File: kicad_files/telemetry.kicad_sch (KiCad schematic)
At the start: 24 parts, among them J10 Conn_ARM_JTAG_SWD_10, J4 RFD900ux 10 Pin Header, J5 RFD900ux 3 Pin Power Select, J6 USB_C_Receptacle_USB2.0_16P, U8 74AHCT125, U9 WE-TVS-82400102

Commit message: reset symbol annotations
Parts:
- renumbered C49 to C43, C52 to C44, C53 to C45, C54 to C46, C55 to C47, C56 to C48, C57 to C49, J4 to J3, J10 to J4, R12 to R10, R13 to R11, R14 to R12, R16 to R13, R17 to R14

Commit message: make schematic changes
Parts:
- removed U8: 74AHCT125, Package_SO:SOIC-14_3.9x8.7mm_P1.27mm, symbol 74xx:74AHCT125
- added U13: 74LVC1G125, Package_TO_SOT_SMD:SOT-23-5, symbol 74xGxx:74LVC1G125
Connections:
- net +5V: now also U13.5 (VCC)
- net GND: now also U13.1, U13.3 (GND)
- net LED_TIM2_CH1: now also U13.2
- net at R10.1: now also U13.4
- no-connect marks 8 -> 5
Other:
- moved on the sheet: C43, C44, D2, D3, R10

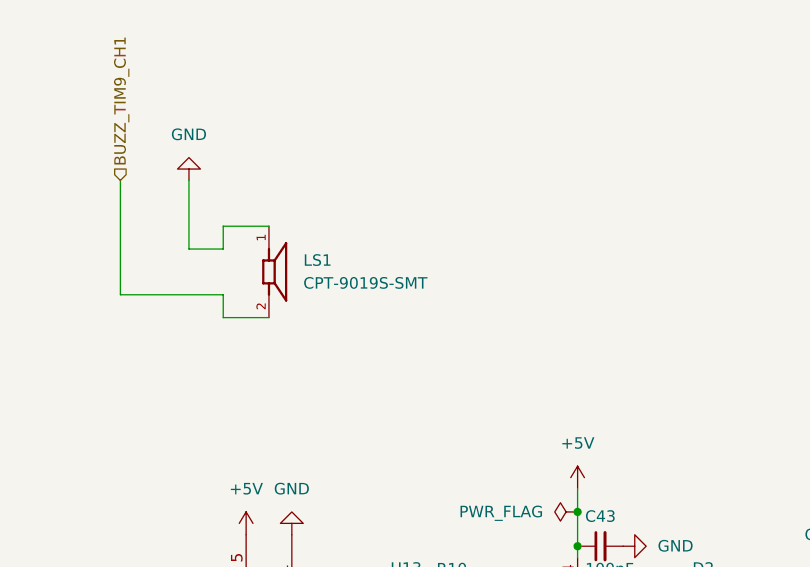
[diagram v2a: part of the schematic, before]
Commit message: Switch buzzer p/n
No footprint yet
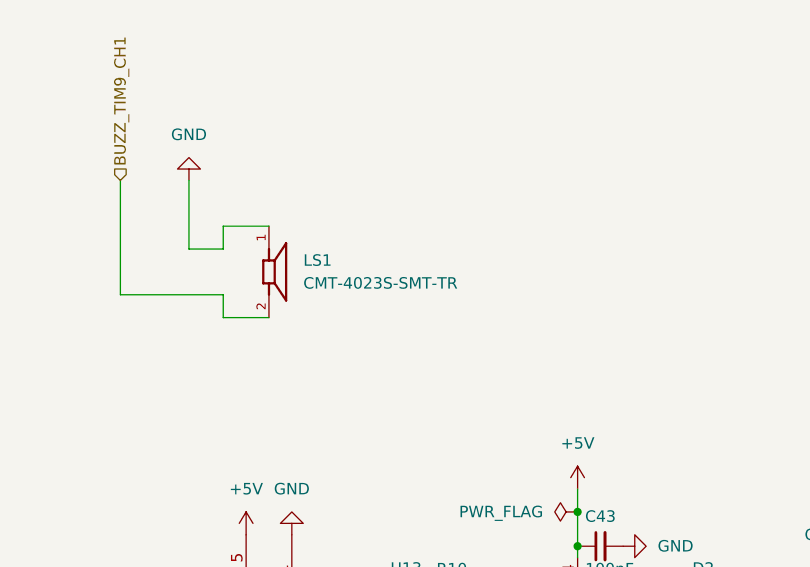
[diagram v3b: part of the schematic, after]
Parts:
- LS1: value CPT-9019S-SMT -> CMT-4023S-SMT-TR; footprint footprints:CUI_CPT-9019S-SMT -> (none)
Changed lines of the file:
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@@
 			)
 		)
-		(property "Value" "CPT-9019S-SMT"
+		(property "Value" "CMT-4023S-SMT-TR"
 			(at 49.53 48.2599 0)
 			(show_name no)
@@
 			)
 		)
-		(property "Footprint" "footprints:CUI_CPT-9019S-SMT"
+		(property "Footprint" ""
 			(at 45.72 46.99 0)
 			(hide yes)

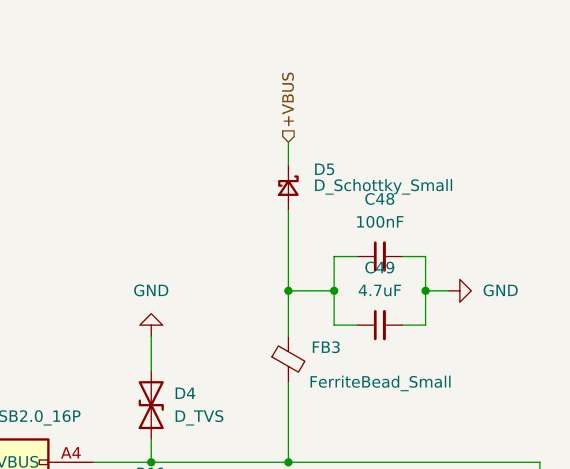
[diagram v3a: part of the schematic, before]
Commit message: VBUS, BMS diodes and fuses
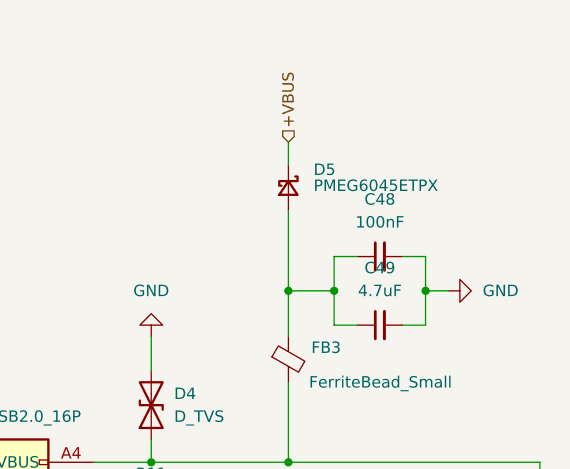
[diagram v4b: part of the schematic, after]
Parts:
- D5: value D_Schottky_Small -> PMEG6045ETPX; footprint (none) -> Diode_SMD:D_SOD-128
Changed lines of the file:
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@@
 			)
 		)
-		(property "Value" "D_Schottky_Small"
+		(property "Value" "PMEG6045ETPX"
 			(at 241.554 36.576 90)
 			(show_name no)
@@
 			)
 		)
-		(property "Footprint" ""
+		(property "Footprint" "Diode_SMD:D_SOD-128"
 			(at 238.76 36.83 90)
 			(hide yes)

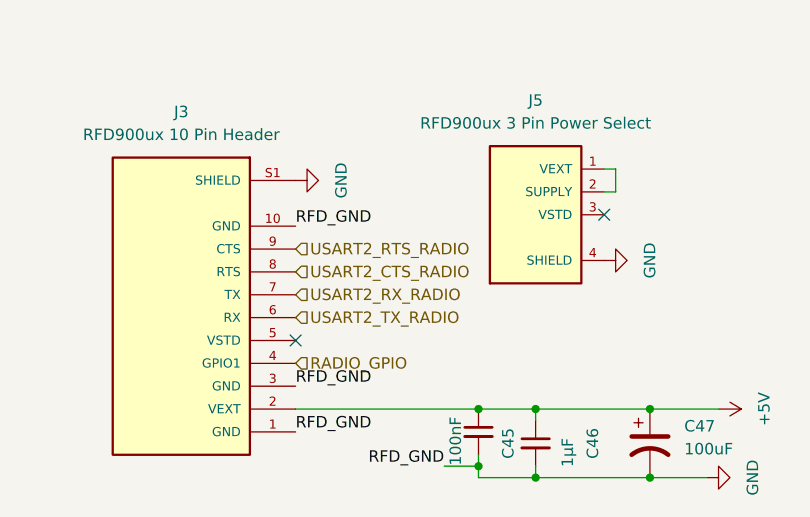
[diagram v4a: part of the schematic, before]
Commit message: switch uart, usart, spi lines, adc, pwm
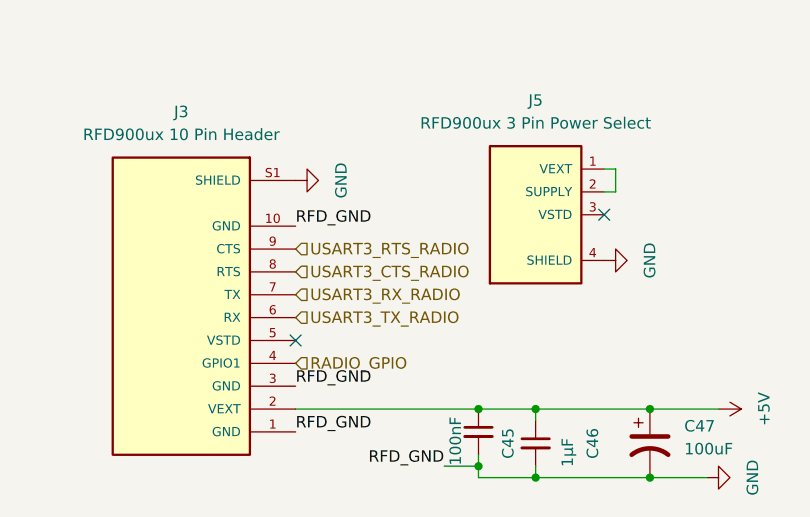
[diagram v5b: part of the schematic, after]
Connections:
- net USART2_CTS_RADIO renamed USART3_CTS_RADIO
- net USART2_RTS_RADIO renamed USART3_RTS_RADIO
- net USART2_RX_RADIO renamed USART3_RX_RADIO
- net USART2_TX_RADIO renamed USART3_TX_RADIO
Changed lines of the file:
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@@
 		)
 	)
-	(hierarchical_label "USART2_RTS_RADIO"
+	(hierarchical_label "USART3_RTS_RADIO"
 		(shape input)
 		(at 119.38 135.89 0)
@@
 		)
 	)
-	(hierarchical_label "USART2_TX_RADIO"
+	(hierarchical_label "USART3_TX_RADIO"
 		(shape input)
 		(at 119.38 143.51 0)
@@
 		)
 	)
-	(hierarchical_label "USART2_RX_RADIO"
+	(hierarchical_label "USART3_RX_RADIO"
 		(shape input)
 		(at 119.38 140.97 0)
@@
 		)
 	)
-	(hierarchical_label "USART2_CTS_RADIO"
+	(hierarchical_label "USART3_CTS_RADIO"
 		(shape input)
 		(at 119.38 138.43 0)

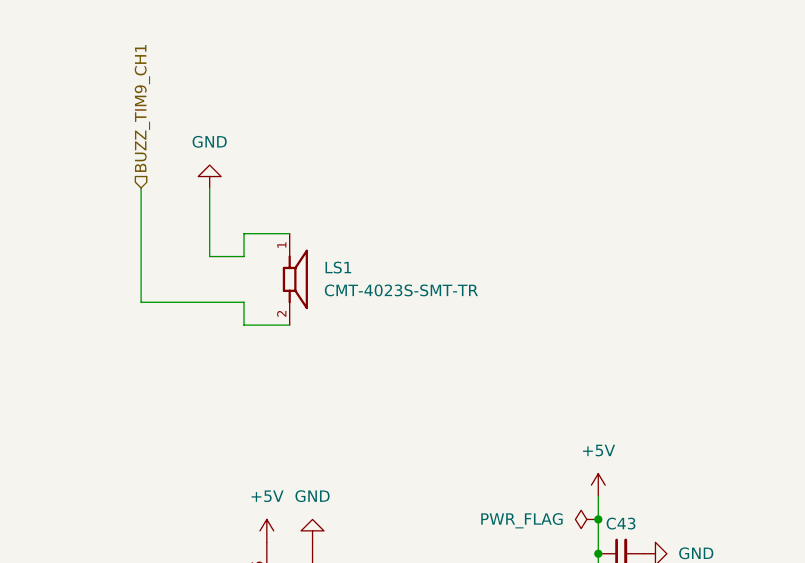
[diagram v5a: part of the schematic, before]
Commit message: complete rest of pin swaps
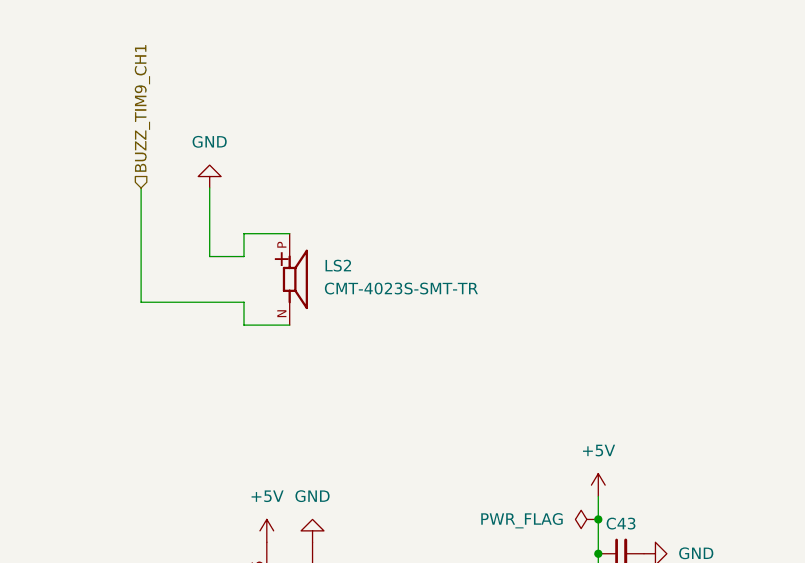
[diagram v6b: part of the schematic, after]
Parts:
- removed LS1: CMT-4023S-SMT-TR, symbol CPT-9019S-SMT:CPT-9019S-SMT
- added LS2: CMT-4023S-SMT-TR, footprints:CUI_CMT-4023S-SMT-TR, symbol CMT-4023S-SMT-TR:CMT-4023S-SMT-TR
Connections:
- net BUZZ_TIM9_CH1: now also LS2.N
- net GND: now also LS2.P
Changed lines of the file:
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@@
-	)
-	(symbol
-		(lib_id "CPT-9019S-SMT:CPT-9019S-SMT")
-		(at 45.72 46.99 0)
-		(unit 1)
-		(body_style 1)
-		(exclude_from_sim no)
-		(in_bom yes)
-		(on_board yes)
-		(in_pos_files yes)
-		(dnp no)
-		(fields_autoplaced yes)
-		(property "Reference" "LS1"
-			(at 49.53 45.7199 0)
-			(show_name no)
-			(do_not_autoplace no)
-			(effects
-				(font
-					(size 1.27 1.27)
-				)
-				(justify left)
-			)
-		)
-		(property "Value" "CMT-4023S-SMT-TR"
-			(at 49.53 48.2599 0)
-			(show_name no)
-			(do_not_autoplace no)
-			(effects
-				(font
-					(size 1.27 1.27)
-				)
-				(justify left)
-			)
-		)
-		(property "Footprint" ""
-			(at 45.72 46.99 0)
-			(hide yes)
-			(show_name no)
-			(do_not_autoplace no)
-			(effects
-				(font
-					(size 1.27 1.27)
-				)
-				(justify bottom)
-			)
-		)
-		(property "Datasheet" ""
-			(at 45.72 46.99 0)
-			(hide yes)
-			(show_name no)
-			(do_not_autoplace no)
-			(effects
-				(font
-					(size 1.27 1.27)
-				)
-			)
-		)
-		(property "Description" ""
-			(at 45.72 46.99 0)
-			(hide yes)
-			(show_name no)
-			(do_not_autoplace no)
-			(effects
-				(font
-					(size 1.27 1.27)
-				)
-			)
-		)
-		(property "MF" "Same Sky"
-			(at 45.72 46.99 0)
-			(hide yes)
-			(show_name no)
-			(do_not_autoplace no)
-			(effects
-				(font
-					(size 1.27 1.27)
-				)
-				(justify bottom)
-			)
-		)
-		(property "Description_1" "9 mm, 25 Vp-p Vdc, 65 dB, Surface Mount (SMT), Piezo Audio Transducer Buzzer"
-			(at 45.72 46.99 0)
-			(hide yes)
-			(show_name no)
-			(do_not_autoplace no)
-			(effects
-				(font
-					(size 1.27 1.27)
-				)
-				(justify bottom)
-			)
-		)
-		(property "Package" "None"
-			(at 45.72 46.99 0)
-			(hide yes)
-			(show_name no)
-			(do_not_autoplace no)
-			(effects
-				(font
-					(size 1.27 1.27)
-				)
-				(justify bottom)
-			)
-		)
-		(property "Price" "None"
-			(at 45.72 46.99 0)
-			(hide yes)
-			(show_name no)
-			(do_not_autoplace no)
-			(effects
-				(font
-					(size 1.27 1.27)
-				)
-				(justify bottom)
-			)
-		)
-		(property "Check_prices" "https://www.snapeda.com/parts/CPT-9019S-SMT-TR/Same+Sky/view-part/?ref=eda"
-			(at 45.72 46.99 0)
-			(hide yes)
-			(show_name no)
-			(do_not_autoplace no)
-			(effects
-				(font
-					(size 1.27 1.27)
-				)
-				(justify bottom)
-			)
-		)
-		(property "PART_REV" "1.0"
-			(at 45.72 46.99 0)
-			(hide yes)
-			(show_name no)
-			(do_not_autoplace no)
-			(effects
-				(font
-					(size 1.27 1.27)
-				)
-				(justify bottom)
-			)
-		)
-		(property "STANDARD" "MANUFACTURER RECOMMENDATIONS"
-			(at 45.72 46.99 0)
-			(hide yes)
-			(show_name no)
-			(do_not_autoplace no)
-			(effects
-				(font
-					(size 1.27 1.27)
-				)
-				(justify bottom)
-			)
-		)
-		(property "SnapEDA_Link" "https://www.snapeda.com/parts/CPT-9019S-SMT-TR/Same+Sky/view-part/?ref=snap"
-			(at 45.72 46.99 0)
-			(hide yes)
-			(show_name no)
-			(do_not_autoplace no)
-			(effects
-				(font
-					(size 1.27 1.27)
-				)
-				(justify bottom)
-			)
-		)
-		(property "MP" "CPT-9019S-SMT-TR"
-			(at 45.72 46.99 0)
-			(hide yes)
-			(show_name no)
-			(do_not_autoplace no)
-			(effects
-				(font
-					(size 1.27 1.27)
-				)
-				(justify bottom)
-			)
-		)
-		(property "Availability" "In Stock"
-			(at 45.72 46.99 0)
-			(hide yes)
-			(show_name no)
-			(do_not_autoplace no)
-			(effects
-				(font
-					(size 1.27 1.27)
-				)
-				(justify bottom)
-			)
-		)
-		(property "MANUFACTURER" "CUI INC"
-			(at 45.72 46.99 0)
-			(hide yes)
-			(show_name no)
-			(do_not_autoplace no)
-			(effects
-				(font
-					(size 1.27 1.27)
-				)
-				(justify bottom)
-			)
-		)
-		(pin "1"
-		)
-		(pin "2"
-		)
-		(instances
-			(project "versorlite"
-				(path "/1a230af0-0a74-48f7-8607-b087121dda49/4d884b5c-b332-4347-90a4-1c2e65497882"
-					(reference "LS1")
-					(unit 1)
-				)
-			)
-		)
 	)
 	(symbol
@@
 					(unit 1)
 				)
+			)
+		)
+	)
+	(symbol
+		(lib_id "CMT-4023S-SMT-TR:CMT-4023S-SMT-TR")
+		(at 45.72 46.99 0)
+		(unit 1)
+		(body_style 1)
+		(exclude_from_sim no)
+		(in_bom yes)
+		(on_board yes)
+		(in_pos_files yes)
+		(dnp no)
+		(fields_autoplaced yes)
+		(property "Reference" "LS2"
+			(at 49.53 45.5097 0)
+			(show_name no)
+			(do_not_autoplace no)
+			(effects
+				(font
+					(size 1.27 1.27)
+				)
+				(justify left)
+			)
+		)
+		(property "Value" "CMT-4023S-SMT-TR"
+			(at 49.53 48.0497 0)
+			(show_name no)
+			(do_not_autoplace no)
+			(effects
+				(font
+					(size 1.27 1.27)
+				)
+				(justify left)
+			)
+		)
+		(property "Footprint" "footprints:CUI_CMT-4023S-SMT-TR"
+			(at 45.72 46.99 0)
+			(hide yes)
+			(show_name no)
+			(do_not_autoplace no)
+			(effects
+				(font
+					(size 1.27 1.27)
+				)
+				(justify bottom)
+			)
+		)
+		(property "Datasheet" ""
+			(at 45.72 46.99 0)
+			(hide yes)
+			(show_name no)
+			(do_not_autoplace no)
+			(effects
+				(font
+					(size 1.27 1.27)
+				)
+			)
+		)
+		(property "Description" "4 mm, 3 Vo-p, 70 dB, Surface Mount (SMT), Magnetic Audio Transducer Buzzer"
+			(at 45.72 46.99 0)
+			(hide yes)
+			(show_name no)
+			(do_not_autoplace no)
+			(effects
+				(font
+					(size 1.27 1.27)
+				)
+				(justify bottom)
+			)
+		)
+		(property "MF" "Same Sky"
+			(at 45.72 46.99 0)
+			(hide yes)
+			(show_name no)
+			(do_not_autoplace no)
+			(effects
+				(font
+					(size 1.27 1.27)
+				)
+				(justify bottom)
+			)
+		)
+		(property "Package" "None"
+			(at 45.72 46.99 0)
+			(hide yes)
+			(show_name no)
+			(do_not_autoplace no)
+			(effects
+				(font
+					(size 1.27 1.27)
+				)
+				(justify bottom)
+			)
+		)
+		(property "Price" "None"
+			(at 45.72 46.99 0)
+			(hide yes)
+			(show_name no)
+			(do_not_autoplace no)
+			(effects
+				(font
+					(size 1.27 1.27)
+				)
+				(justify bottom)
+			)
+		)
+		(property "Check_prices" "https://www.snapeda.com/parts/CMT-4023S-SMT-TR/Same+Sky/view-part/?ref=eda"
+			(at 45.72 46.99 0)
+			(hide yes)
+			(show_name no)
+			(do_not_autoplace no)
+			(effects
+				(font
+					(size 1.27 1.27)
+				)
+				(justify bottom)
+			)
+		)
+		(property "STANDARD" "Manufacturer recommendations"
+			(at 45.72 46.99 0)
+			(hide yes)
+			(show_name no)
+			(do_not_autoplace no)
+			(effects
+				(font
+					(size 1.27 1.27)
+				)
+				(justify bottom)
+			)
+		)
+		(property "PARTREV" "1.0"
+			(at 45.72 46.99 0)
+			(hide yes)
+			(show_name no)
+			(do_not_autoplace no)
+			(effects
+				(font
+					(size 1.27 1.27)
+				)
+				(justify bottom)
+			)
+		)
+		(property "SnapEDA_Link" "https://www.snapeda.com/parts/CMT-4023S-SMT-TR/Same+Sky/view-part/?ref=snap"
+			(at 45.72 46.99 0)
+			(hide yes)
+			(show_name no)
+			(do_not_autoplace no)
+			(effects
+				(font
+					(size 1.27 1.27)
+				)
+				(justify bottom)
+			)
+		)
+		(property "MP" "CMT-4023S-SMT-TR"
+			(at 45.72 46.99 0)
+			(hide yes)
+			(show_name no)
+			(do_not_autoplace no)
+			(effects
+				(font
+					(size 1.27 1.27)
+				)
+				(justify bottom)
+			)
+		)
+		(property "Availability" "In Stock"
+			(at 45.72 46.99 0)
+			(hide yes)
+			(show_name no)
+			(do_not_autoplace no)
+			(effects
+				(font
+					(size 1.27 1.27)
+				)
+				(justify bottom)
+			)
+		)
+		(property "MANUFACTURER" "CUI INC"
+			(at 45.72 46.99 0)
+			(hide yes)
+			(show_name no)
+			(do_not_autoplace no)
+			(effects
+				(font
+					(size 1.27 1.27)
+				)
+				(justify bottom)
+			)
+		)
+		(pin "P"
+		)
+		(pin "N"
+		)
+		(instances
+			(project "versorlite"
+				(path "/1a230af0-0a74-48f7-8607-b087121dda49/4d884b5c-b332-4347-90a4-1c2e65497882"
+					(reference "LS2")
+					(unit 1)
+				)

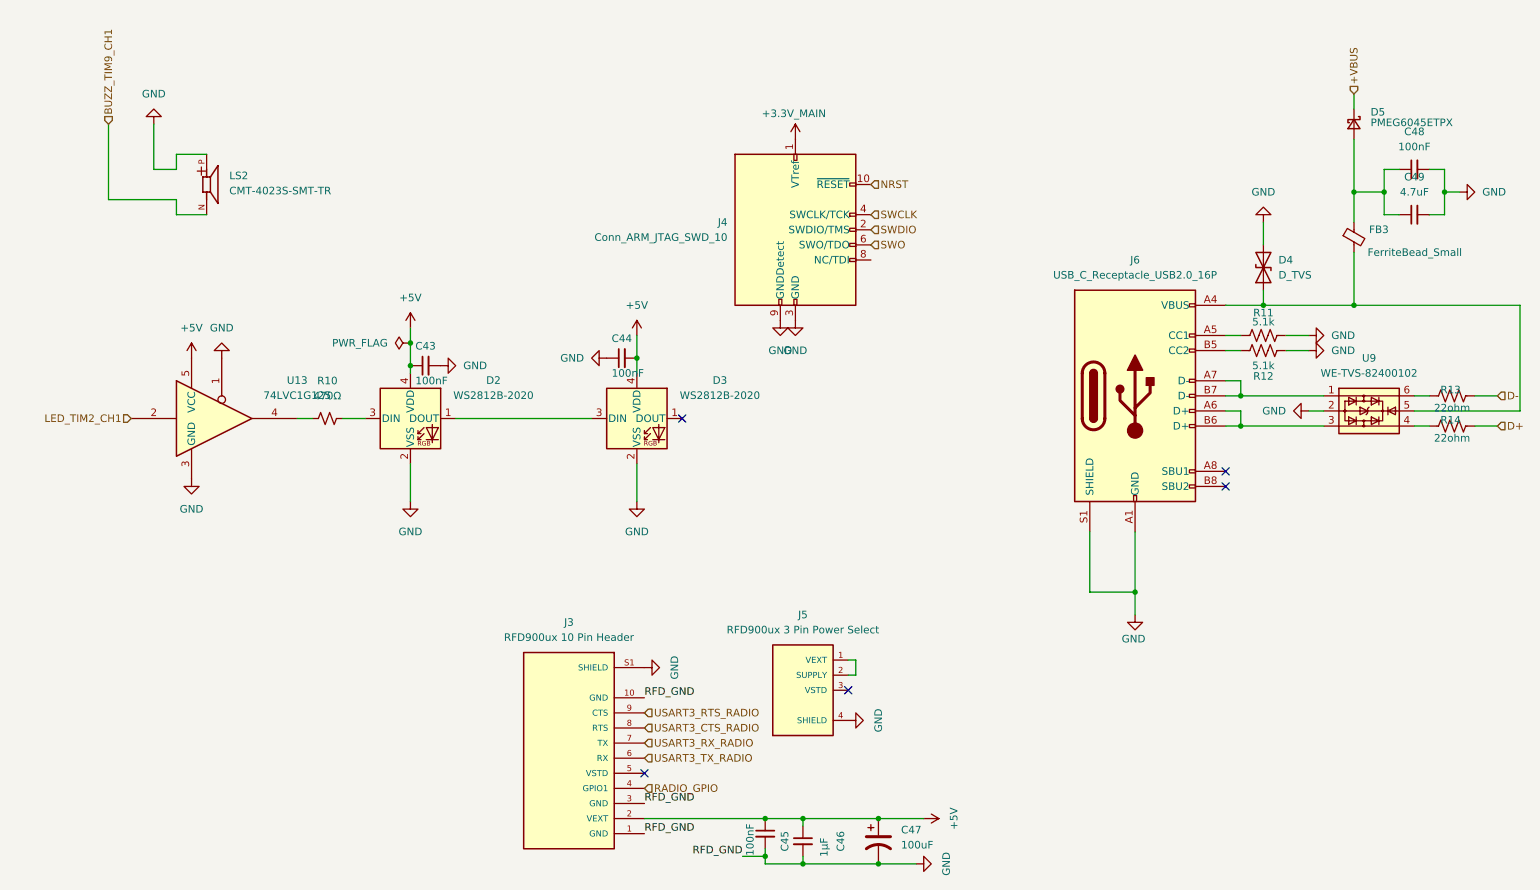
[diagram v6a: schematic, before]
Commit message: add dedicated power switching
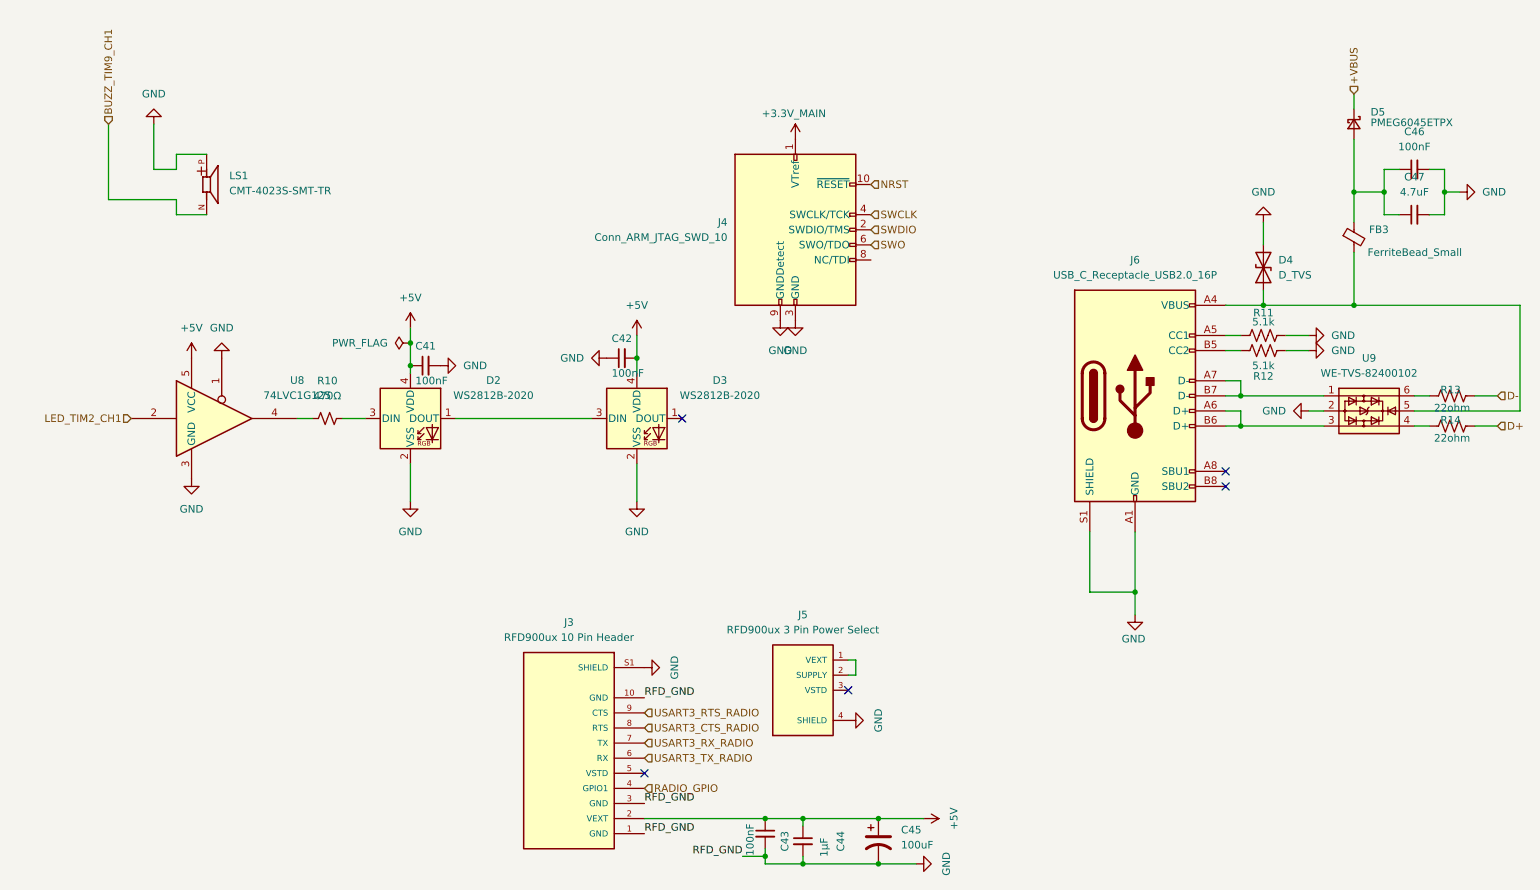
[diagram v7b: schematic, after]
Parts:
- renumbered C43 to C41, C44 to C42, C45 to C43, C46 to C44, C47 to C45, C48 to C46, C49 to C47, LS2 to LS1, U13 to U8
